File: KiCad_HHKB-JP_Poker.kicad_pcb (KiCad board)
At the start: 2 copper layers, 285 x 95.1 mm, 158 parts, among them SW1 SW_Push, U1 ATmega32U4-MU, U2 PRTR5V0U2X, Y1 16MHz

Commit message: R4(space列)の配置完了
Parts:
- removed the D42 at (292.4, 286.1)
- removed K_LGUI1: MX-NoLED, MX_Only:MXOnly-1U-Hotswap
- moved D10 84.1 mm to (246.1, 260.4)
- moved D43 77.8 mm to (390.1, 243.9), turned to 90 degrees
- moved K_WIN1 66.7 mm to (300.8, 258.0)
- moved K_LSPACE1 65.5 mm to (236.5, 258.0)
- moved D37 52.1 mm to (290.1, 259.6), turned to 90 degrees
- moved D42 49.5 mm to (309.2, 259.6), turned to 90 degrees
- moved K_HENK1 45.6 mm to (281.8, 258.0)
- moved K_RSPACE1 42.8 mm to (260.4, 258.0)
- moved D11 35.2 mm to (174.6, 293.7)
- moved D16 19.1 mm to (204.0, 259.6)
- moved K_LALT1 19.1 mm to (196.1, 258.0)
- moved D1 16.7 mm to (223.0, 259.6)
- moved K_NHENK1 16.7 mm to (215.1, 258.0)
- moved D27 4.76 mm to (389.7, 259.6)
- moved D63 4.76 mm to (370.7, 259.6)
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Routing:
- net Net-(D11-Pad2): track 5.89 -> 0.00 mm
- net COL1: track 65.6 -> 61.2 mm, vias 5 -> 4

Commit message: Diodeの配置完了
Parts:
- removed the D10 at (311.1, 295.4)
- removed the D11 at (174.6, 293.7)
- moved D11 69.3 mm to (269.9, 260.4), turned to 90 degrees
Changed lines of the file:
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@@
-  )
-  (footprint "Diode_SMD:D_SOD-123" (layer "B.Cu")
-    (at 174.625 293.6875 90)
-    (descr "SOD-123")
-    (tags "SOD-123")
-    (attr smd)
-    (fp_text reference "D11" (at 0 2 90) (layer "B.SilkS")
-      (effects (font (size 1 1) (thickness 0.15)) (justify mirror))
-    )
-    (fp_text value "SOD-123" (at 0 -2.1 90) (layer "B.Fab")
-      (effects (font (size 1 1) (thickness 0.15)) (justify mirror))
-    )
-    (fp_text user "${REFERENCE}" (at 0 2 90) (layer "B.Fab")
-      (effects (font (size 1 1) (thickness 0.15)) (justify mirror))
-    )
-    (fp_line (start -2.25 1) (end -2.25 -1) (layer "B.SilkS") (width 0.12))
-    (fp_line (start -2.25 1) (end 1.65 1) (layer "B.SilkS") (width 0.12))
-    (fp_line (start -2.25 -1) (end 1.65 -1) (layer "B.SilkS") (width 0.12))
-    (fp_line (start -2.35 1.15) (end -2.35 -1.15) (layer "B.CrtYd") (width 0.05))
-    (fp_line (start 2.35 -1.15) (end -2.35 -1.15) (layer "B.CrtYd") (width 0.05))
-    (fp_line (start 2.35 1.15) (end 2.35 -1.15) (layer "B.CrtYd") (width 0.05))
-    (fp_line (start -2.35 1.15) (end 2.35 1.15) (layer "B.CrtYd") (width 0.05))
-    (fp_line (start 1.4 0.9) (end 1.4 -0.9) (layer "B.Fab") (width 0.1))
-    (fp_line (start 0.25 0) (end 0.75 0) (layer "B.Fab") (width 0.1))
-    (fp_line (start -1.4 -0.9) (end -1.4 0.9) (layer "B.Fab") (width 0.1))
-    (fp_line (start -0.35 0) (end -0.35 0.55) (layer "B.Fab") (width 0.1))
-    (fp_line (start -0.35 0) (end 0.25 0.4) (layer "B.Fab") (width 0.1))
-    (fp_line (start 0.25 0.4) (end 0.25 -0.4) (layer "B.Fab") (width 0.1))
-    (fp_line (start -0.75 0) (end -0.35 0) (layer "B.Fab") (width 0.1))
-    (fp_line (start -1.4 0.9) (end 1.4 0.9) (layer "B.Fab") (width 0.1))
-    (fp_line (start 0.25 -0.4) (end -0.35 0) (layer "B.Fab") (width 0.1))
-    (fp_line (start 1.4 -0.9) (end -1.4 -0.9) (layer "B.Fab") (width 0.1))
-    (fp_line (start -0.35 0) (end -0.35 -0.55) (layer "B.Fab") (width 0.1))
-    (pad "1" smd rect locked (at -1.65 0 90) (size 0.9 1.2) (layers "B.Cu" "B.Paste" "B.Mask")
-      (net 38 "ROW4"))
-    (pad "2" smd rect locked (at 1.65 0 90) (size 0.9 1.2) (layers "B.Cu" "B.Paste" "B.Mask")
-      (net 15 "Net-(D11-Pad2)"))
-    (model "${KISYS3DMOD}/Diode_SMD.3dshapes/D_SOD-123.wrl"
-      (offset (xyz 0 0 0))
-      (scale (xyz 1 1 1))
-      (rotate (xyz 0 0 0))
-    )
   )
   (footprint "Diode_SMD:D_SOD-123" (layer "B.Cu")
@@
   )
   (footprint "Diode_SMD:D_SOD-123" (layer "B.Cu")
-    (at 324.139 303.403 180)
+    (at 269.875 260.35 90)
     (descr "SOD-123")
     (tags "SOD-123")
@@
     (property "Sheetname" "matrix")
     (attr smd)
-    (fp_text reference "D11" (at 0 2) (layer "B.SilkS")
-      (effects (font (size 1 1) (thickness 0.15)) (justify mirror))
-    )
-    (fp_text value "SOD-123" (at 0 -2.1) (layer "B.Fab")
-      (effects (font (size 1 1) (thickness 0.15)) (justify mirror))
-    )
-    (fp_text user "${REFERENCE}" (at 0 2) (layer "B.Fab")
+    (fp_text reference "D11" (at 0 2 90) (layer "B.SilkS")
+      (effects (font (size 1 1) (thickness 0.15)) (justify mirror))
+    )
+    (fp_text value "SOD-123" (at 0 -2.1 90) (layer "B.Fab")
+      (effects (font (size 1 1) (thickness 0.15)) (justify mirror))
+    )
+    (fp_text user "${REFERENCE}" (at 0 2 90) (layer "B.Fab")
       (effects (font (size 1 1) (thickness 0.15)) (justify mirror))
     )
@@
     (fp_line (start 1.4 -0.9) (end -1.4 -0.9) (layer "B.Fab") (width 0.1))
     (fp_line (start -1.4 0.9) (end 1.4 0.9) (layer "B.Fab") (width 0.1))
-    (pad "1" smd rect (at -1.65 0 180) (size 0.9 1.2) (layers "B.Cu" "B.Paste" "B.Mask")
+    (pad "1" smd rect (at -1.65 0 90) (size 0.9 1.2) (layers "B.Cu" "B.Paste" "B.Mask")
       (net 38 "ROW4") (pinfunction "K") (pintype "passive"))
-    (pad "2" smd rect (at 1.65 0 180) (size 0.9 1.2) (layers "B.Cu" "B.Paste" "B.Mask")
+    (pad "2" smd rect (at 1.65 0 90) (size 0.9 1.2) (layers "B.Cu" "B.Paste" "B.Mask")
       (net 15 "Net-(D11-Pad2)") (pinfunction "A") (pintype "passive"))
     (model "${KICAD6_3DMODEL_DIR}/Diode_SMD.3dshapes/D_SOD-123.wrl"
       (offset (xyz 0 0 0))
-      (scale (xyz 1 1 1))
-      (rotate (xyz 0 0 0))
-    )
-  )
-  (footprint "Diode_SMD:D_SOD-123" (layer "B.Cu")
-    (at 311.15 295.402 180)
-    (descr "SOD-123")
-    (tags "SOD-123")
-    (property "Sheetfile" "matrix.kicad_sch")
-    (property "Sheetname" "matrix")
-    (attr smd)
-    (fp_text reference "D10" (at 0 2) (layer "B.SilkS")
-      (effects (font (size 1 1) (thickness 0.15)) (justify mirror))
-    )
-    (fp_text value "SOD-123" (at 0 -2.1) (layer "B.Fab")
-      (effects (font (size 1 1) (thickness 0.15)) (justify mirror))
-    )
-    (fp_text user "${REFERENCE}" (at 0 2) (layer "B.Fab")
-      (effects (font (size 1 1) (thickness 0.15)) (justify mirror))
-    )
-    (fp_line (start -2.25 1) (end 1.65 1) (layer "B.SilkS") (width 0.12))
-    (fp_line (start -2.25 -1) (end 1.65 -1) (layer "B.SilkS") (width 0.12))
-    (fp_line (start -2.25 1) (end -2.25 -1) (layer "B.SilkS") (width 0.12))
-    (fp_line (start -2.35 1.15) (end -2.35 -1.15) (layer "B.CrtYd") (width 0.05))
-    (fp_line (start 2.35 -1.15) (end -2.35 -1.15) (layer "B.CrtYd") (width 0.05))
-    (fp_line (start -2.35 1.15) (end 2.35 1.15) (layer "B.CrtYd") (width 0.05))
-    (fp_line (start 2.35 1.15) (end 2.35 -1.15) (layer "B.CrtYd") (width 0.05))
-    (fp_line (start 0.25 0.4) (end 0.25 -0.4) (layer "B.Fab") (width 0.1))
-    (fp_line (start -0.75 0) (end -0.35 0) (layer "B.Fab") (width 0.1))
-    (fp_line (start -1.4 0.9) (end 1.4 0.9) (layer "B.Fab") (width 0.1))
-    (fp_line (start -0.35 0) (end -0.35 0.55) (layer "B.Fab") (width 0.1))
-    (fp_line (start 0.25 0) (end 0.75 0) (layer "B.Fab") (width 0.1))
-    (fp_line (start 0.25 -0.4) (end -0.35 0) (layer "B.Fab") (width 0.1))
-    (fp_line (start 1.4 -0.9) (end -1.4 -0.9) (layer "B.Fab") (width 0.1))
-    (fp_line (start -0.35 0) (end -0.35 -0.55) (layer "B.Fab") (width 0.1))
-    (fp_line (start -0.35 0) (end 0.25 0.4) (layer "B.Fab") (width 0.1))
-    (fp_line (start 1.4 0.9) (end 1.4 -0.9) (layer "B.Fab") (width 0.1))
-    (fp_line (start -1.4 -0.9) (end -1.4 0.9) (layer "B.Fab") (width 0.1))
-    (pad "1" smd rect (at -1.65 0 180) (size 0.9 1.2) (layers "B.Cu" "B.Paste" "B.Mask")
-      (net 38 "ROW4") (pinfunction "K") (pintype "passive"))
-    (pad "2" smd rect (at 1.65 0 180) (size 0.9 1.2) (layers "B.Cu" "B.Paste" "B.Mask")
-      (net 97 "Net-(D10-Pad2)") (pinfunction "A") (pintype "passive"))
-    (model "${KICAD6_3DMODEL_DIR}/Diode_SMD.3dshapes/D_SOD-123.wrl"
-      (offset (xyz 0 0 0))

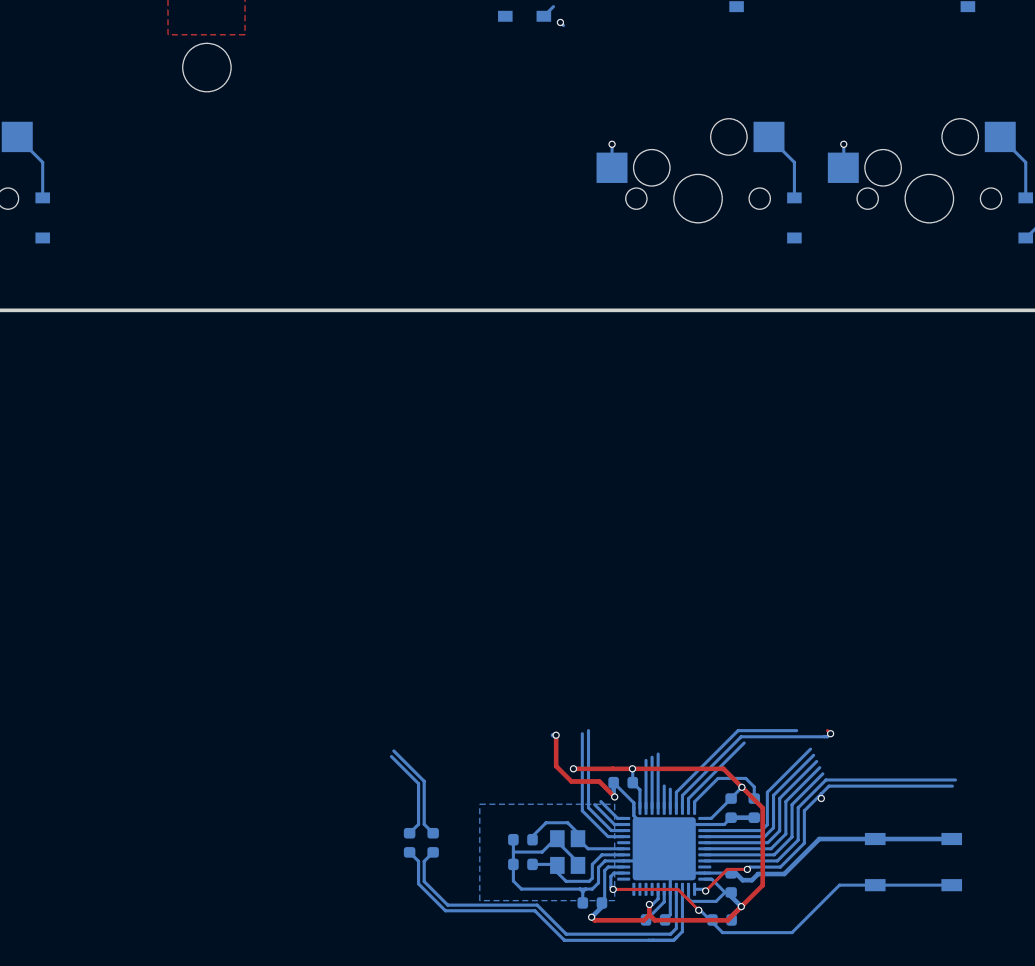
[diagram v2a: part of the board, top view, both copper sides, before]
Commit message: MCUの配置完了
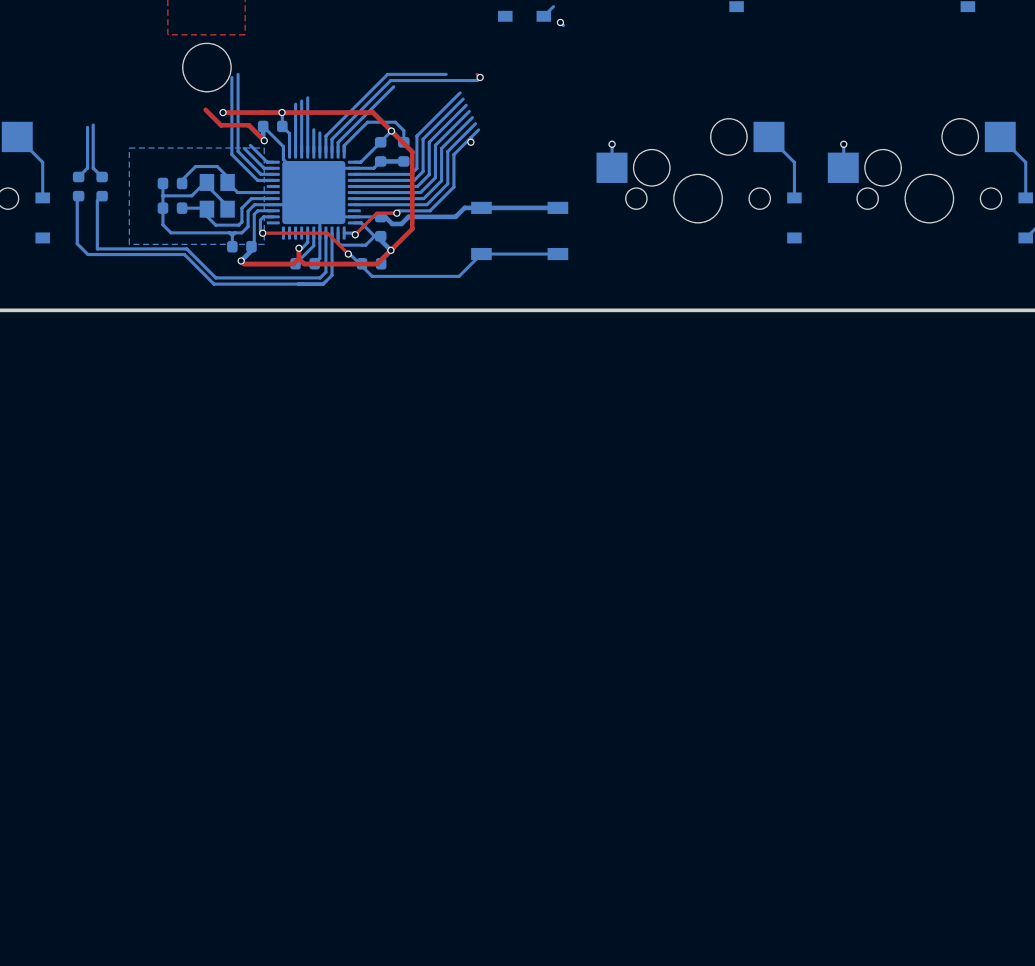
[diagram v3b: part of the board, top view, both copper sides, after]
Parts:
- moved C3 61.3 mm to (158.5, 261.9)
- moved C5 61.3 mm to (152.8, 256.7)
- moved R4 61.3 mm to (171.8, 254.1)
- moved Y1 61.3 mm to (156.5, 257.7)
- moved C2 61.3 mm to (169.9, 254.1)
- moved U1 61.3 mm to (164.4, 257.5)
- moved C1 61.3 mm to (161.0, 252.0)
- moved C6 61.3 mm to (152.8, 258.8)
- moved C7 61.3 mm to (163.7, 263.3)
- moved R5 61.3 mm to (169.2, 263.3)
- moved C4 61.3 mm to (169.9, 260.3)
- moved SW1 61.3 mm to (181.4, 260.6)
- moved R1 60.5 mm to (147.0, 257.0)
- moved R3 60.5 mm to (145.0, 257.0)
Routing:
- net COL7: track 77.3 -> 66.7 mm
- net ROW4: track 62.2 -> 52.0 mm
- net GND: track 172.3 -> 165.3 mm, vias 5 -> 4
- net Net-(R5-Pad1): track 33.4 -> 29.0 mm
- net D+: track 55.5 -> 52.0 mm
- net D-: track 54.8 -> 51.6 mm
- net USB+: track 28.7 -> 27.7 mm

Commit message: 配線途中1
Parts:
- K_RIGHT1: footprint MX_Only:MXOnly-1U-Hotswap -> MX_Only:MXOnly-1.25U-Hotswap
- moved D10 1.08 mm to (245.3, 259.6)
- moved D11 1.02 mm to (270.1, 259.4)
- moved R1 0.32 mm to (147.2, 256.8)
- moved R3 0.32 mm to (145.3, 256.8)
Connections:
- U1 pad 19: COL1 -> COL0
- U1 pad 20: COL0 -> COL1
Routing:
- net ROW4: track 52.0 -> 334.8 mm, vias 6 -> 5
- net ROW3: track 5.59 -> 238.9 mm
- net COL2: track 57.4 -> 131.8 mm, vias 5 -> 6
- net COL0: track 50.2 -> 113.7 mm, vias 4 -> 7
- net COL3: track 57.2 -> 101.5 mm, vias 6 -> 5
- net COL5: track 58.0 -> 99.7 mm, vias 4 -> 5
- net COL4: track 56.3 -> 97.4 mm, vias 4 -> 5
- net D+: track 52.0 -> 87.5 mm
- net D-: track 51.6 -> 87.2 mm
- net COL1: track 61.2 -> 95.3 mm
- net Net-(D74-Pad2): track 1.26 -> 26.2 mm
- net Net-(D11-Pad2): track 0.00 -> 6.42 mm
- net Net-(D10-Pad2): track 0.00 -> 6.28 mm
- net Net-(D37-Pad2): track 0.00 -> 6.22 mm
- net Net-(D42-Pad2): track 0.00 -> 6.16 mm
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
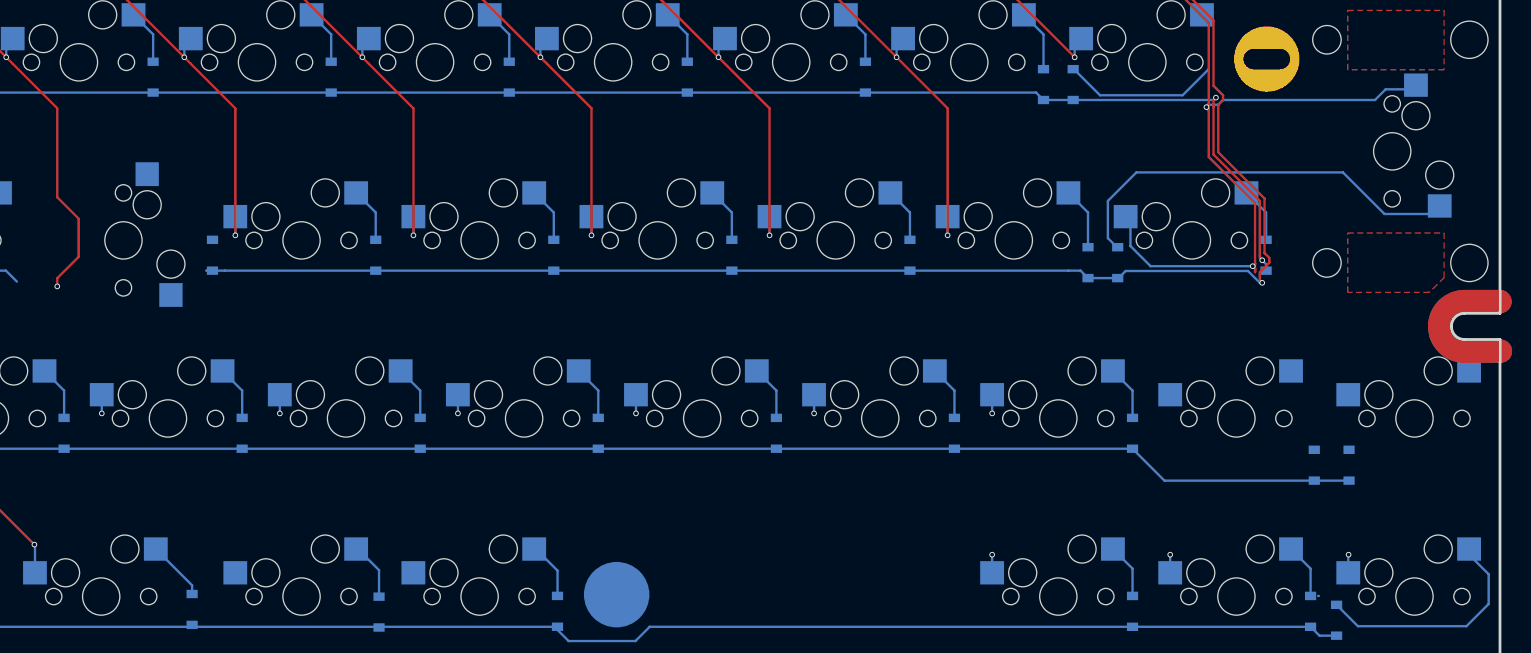
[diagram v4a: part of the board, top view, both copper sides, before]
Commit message: colの配線完了
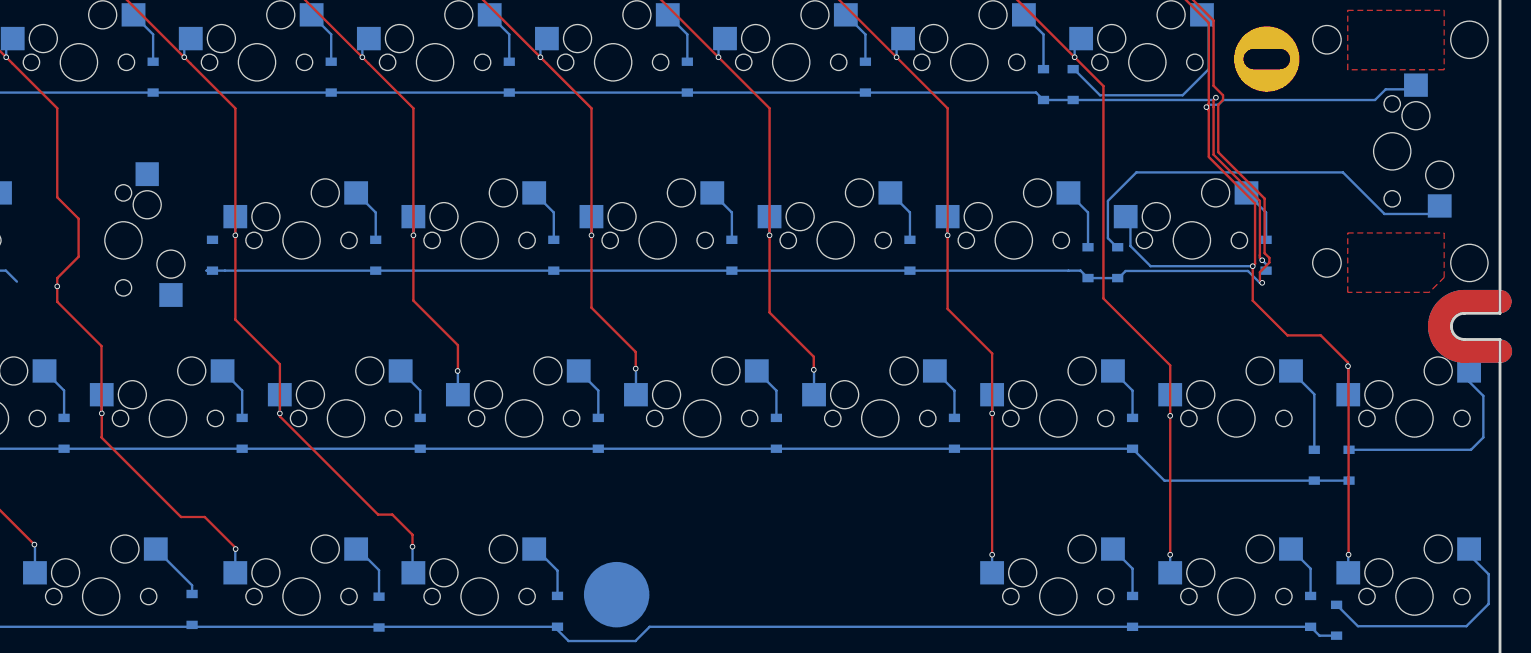
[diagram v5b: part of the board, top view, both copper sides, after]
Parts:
- K_RIGHT1: footprint MX_Only:MXOnly-1.25U-Hotswap -> MX_Only:MXOnly-1U-Hotswap
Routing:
- net COL12: track 90.8 -> 148.0 mm, vias 6 -> 7
- net COL7: track 66.7 -> 111.5 mm, vias 4 -> 5
- net COL6: track 75.2 -> 115.2 mm, vias 5 -> 6
- net COL13: track 99.9 -> 138.5 mm, vias 4 -> 5
- net COL11: track 67.6 -> 103.7 mm
- net Net-(D67-Pad2): track 1.17 -> 23.7 mm
- net COL8: track 66.4 -> 83.5 mm
- net COL9: track 66.2 -> 83.2 mm
- net COL10: track 65.9 -> 82.9 mm
- net Net-(D43-Pad2): track 0.00 -> 9.46 mm

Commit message: 時間的にいったんここまで
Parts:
- K_RIGHT1: footprint MX_Only:MXOnly-1U-Hotswap -> MX_Only:MXOnly-1.25U-Hotswap
- moved D35 2.07 mm to (270.2, 221.4)
- turned K_H1 to 0 degrees
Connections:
- D35 pad 2: Net-(D35-Pad2) -> Net-(K_H1-Pad2)
- K_H1 pad 1: Net-(D35-Pad2) -> COL6
- K_H1 pad 2: COL6 -> Net-(K_H1-Pad2)
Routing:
- net COL13: track 138.5 -> 364.7 mm
- net COL12: track 148.0 -> 352.6 mm
- net COL11: track 103.7 -> 287.3 mm
- net COL10: track 82.9 -> 260.7 mm, vias 4 -> 5
- net COL9: track 83.2 -> 240.9 mm, vias 4 -> 5
- net COL8: track 83.5 -> 222.2 mm, vias 4 -> 5
- net ROW1: track 252.0 -> 374.8 mm, vias 3 -> 4
- net COL7: track 111.5 -> 229.3 mm
- net ROW0: track 283.0 -> 394.9 mm, vias 1 -> 2
- net COL6: track 115.2 -> 203.6 mm
- net GND: track 165.3 -> 209.1 mm, vias 4 -> 5
- net Net-(D5-Pad2): track 0.16 -> 38.0 mm, vias 0 -> 2
- net +5V: track 113.0 -> 150.7 mm
- net ROW2: track 257.4 -> 293.3 mm
- net ROW3: track 238.9 -> 229.4 mm
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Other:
- rule pad_to_mask_clearance: 0.2 -> 0.25

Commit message: 縦（Col）の配線完了
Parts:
- moved D64 0.10 mm to (392.9, 184.2)
- renumbered C5 to C1, C6 to C2, C7 to C3, C1 to C4, C2 to C5, C3 to C6, C4 to C7, D32 to D1, D15 to D10, D12 to D11, D13 to D12, D14 to D13, D21 to D14, D16 to D15, D18 to D16, D19 to D17, D20 to D18, D26 to D19, D1 to D20, D23 to D21, D24 to D22, D25 to D23, D31 to D24, D10 to D25, D28 to D26, D29 to D27, D30 to D28, D36 to D29, D11 to D30, D37 to D31, D33 to D32, D34 to D33, D35 to D34, D41 to D35, D42 to D36, D38 to D37, D39 to D38, D40 to D39, D47 to D40, D44 to D41, D45 to D42, D46 to D43, D52 to D44, D49 to D45, D50 to D46, D51 to D47, D57 to D48, D54 to D49, D55 to D50, D56 to D51, D62 to D52, D59 to D53, D60 to D54, D61 to D55, D22 to D56, D63 to D57, D65 to D58, D66 to D59, D71 to D60, D43 to D61, D27 to D62, D70 to D63, D17 to D64, D72 to D65, D67 to D66, D74 to D67, K_UNSC1 to K_BKSL1, K_PIPE1 to K_YEN1, K_]2 to K_]1, R3 to R2, R5 to R3, R2 to R4, R6 to R5, R4 to R6
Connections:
- D60 pad 1: ROW1 -> ROW2
- D64 pad 1: ROW2 -> ROW1
- K_BKSPC1 pad 1: COL12 -> COL13
- K_]1 pad 1: COL13 -> COL12
- U1 pad 21: COL2 -> unconnected-(U1-Pad21)
- U1 pad 22: COL3 -> unconnected-(U1-Pad22)
- U1 pad 25: COL4 -> unconnected-(U1-Pad25)
- U1 pad 26: COL5 -> unconnected-(U1-Pad26)
- U1 pad 27: ROW3 -> unconnected-(U1-Pad27)
- U1 pad 28: ROW2 -> unconnected-(U1-Pad28)
- U1 pad 29: ROW1 -> unconnected-(U1-Pad29)
- U1 pad 30: ROW0 -> unconnected-(U1-Pad30)
- U1 pad 31: COL6 -> unconnected-(U1-Pad31)
- U1 pad 32: COL13 -> unconnected-(U1-Pad32)
- U1 pad 36: COL12 -> unconnected-(U1-Pad36)
- U1 pad 37: COL11 -> unconnected-(U1-Pad37)
- U1 pad 38: COL10 -> unconnected-(U1-Pad38)
- U1 pad 39: COL9 -> unconnected-(U1-Pad39)
- U1 pad 40: COL8 -> unconnected-(U1-Pad40)
- U1 pad 41: COL7 -> unconnected-(U1-Pad41)
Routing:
- net COL12: track 352.6 -> 89.8 mm, vias 7 -> 5
- net COL13: track 364.7 -> 135.0 mm, vias 5 -> 4
- net COL11: track 287.3 -> 90.7 mm
- net COL10: track 260.7 -> 69.4 mm, vias 5 -> 4
- net COL9: track 240.9 -> 69.4 mm, vias 5 -> 4
- net ROW0: track 394.9 -> 227.6 mm, vias 2 -> 0
- net COL8: track 222.2 -> 69.4 mm, vias 5 -> 4
- net ROW1: track 374.8 -> 236.3 mm, vias 4 -> 2
- net COL7: track 229.3 -> 97.2 mm
- net COL6: track 203.6 -> 98.5 mm, vias 6 -> 5
- net unconnected-(U1-Pad29): track 0.00 -> 95.6 mm
- net ROW2: track 293.3 -> 214.0 mm, vias 3 -> 1
- net COL2: track 131.8 -> 92.4 mm, vias 6 -> 5
- net ROW4: track 329.0 -> 295.2 mm, vias 4 -> 2
- net unconnected-(U1-Pad21): track 0.00 -> 31.7 mm
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
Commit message: key switch 間の配線は完了。これから、Key Switch と MCUを使う
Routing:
- net unconnected-(U1-Pad29): track 95.6 -> 11.4 mm
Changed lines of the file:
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@@
   (segment (start 164.909375 252.539625) (end 171.831 245.618) (width 0.254) (layer "B.Cu") (net 116))
   (segment (start 164.909375 254.13125) (end 164.909375 252.539625) (width 0.254) (layer "B.Cu") (net 116))
-  (segment (start 171.831 245.618) (end 256.032 245.618) (width 0.254) (layer "B.Cu") (net 116))
   (segment (start 165.409375 254.13125) (end 165.409375 252.801625) (width 0.254) (layer "B.Cu") (net 117))
   (segment (start 165.409375 252.801625) (end 172.085 246.126) (width 0.254) (layer "B.Cu") (net 117))
